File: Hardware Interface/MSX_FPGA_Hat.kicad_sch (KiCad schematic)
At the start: 24 parts, among them J1 J1, J2 J2, J3a1 J3a, J3b1 J3b, J4a1 J4a, J4b1 J4b, U1 74LVC245A, U2 74LVC245A, U3 74LVC245A, U4 74LVC245A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

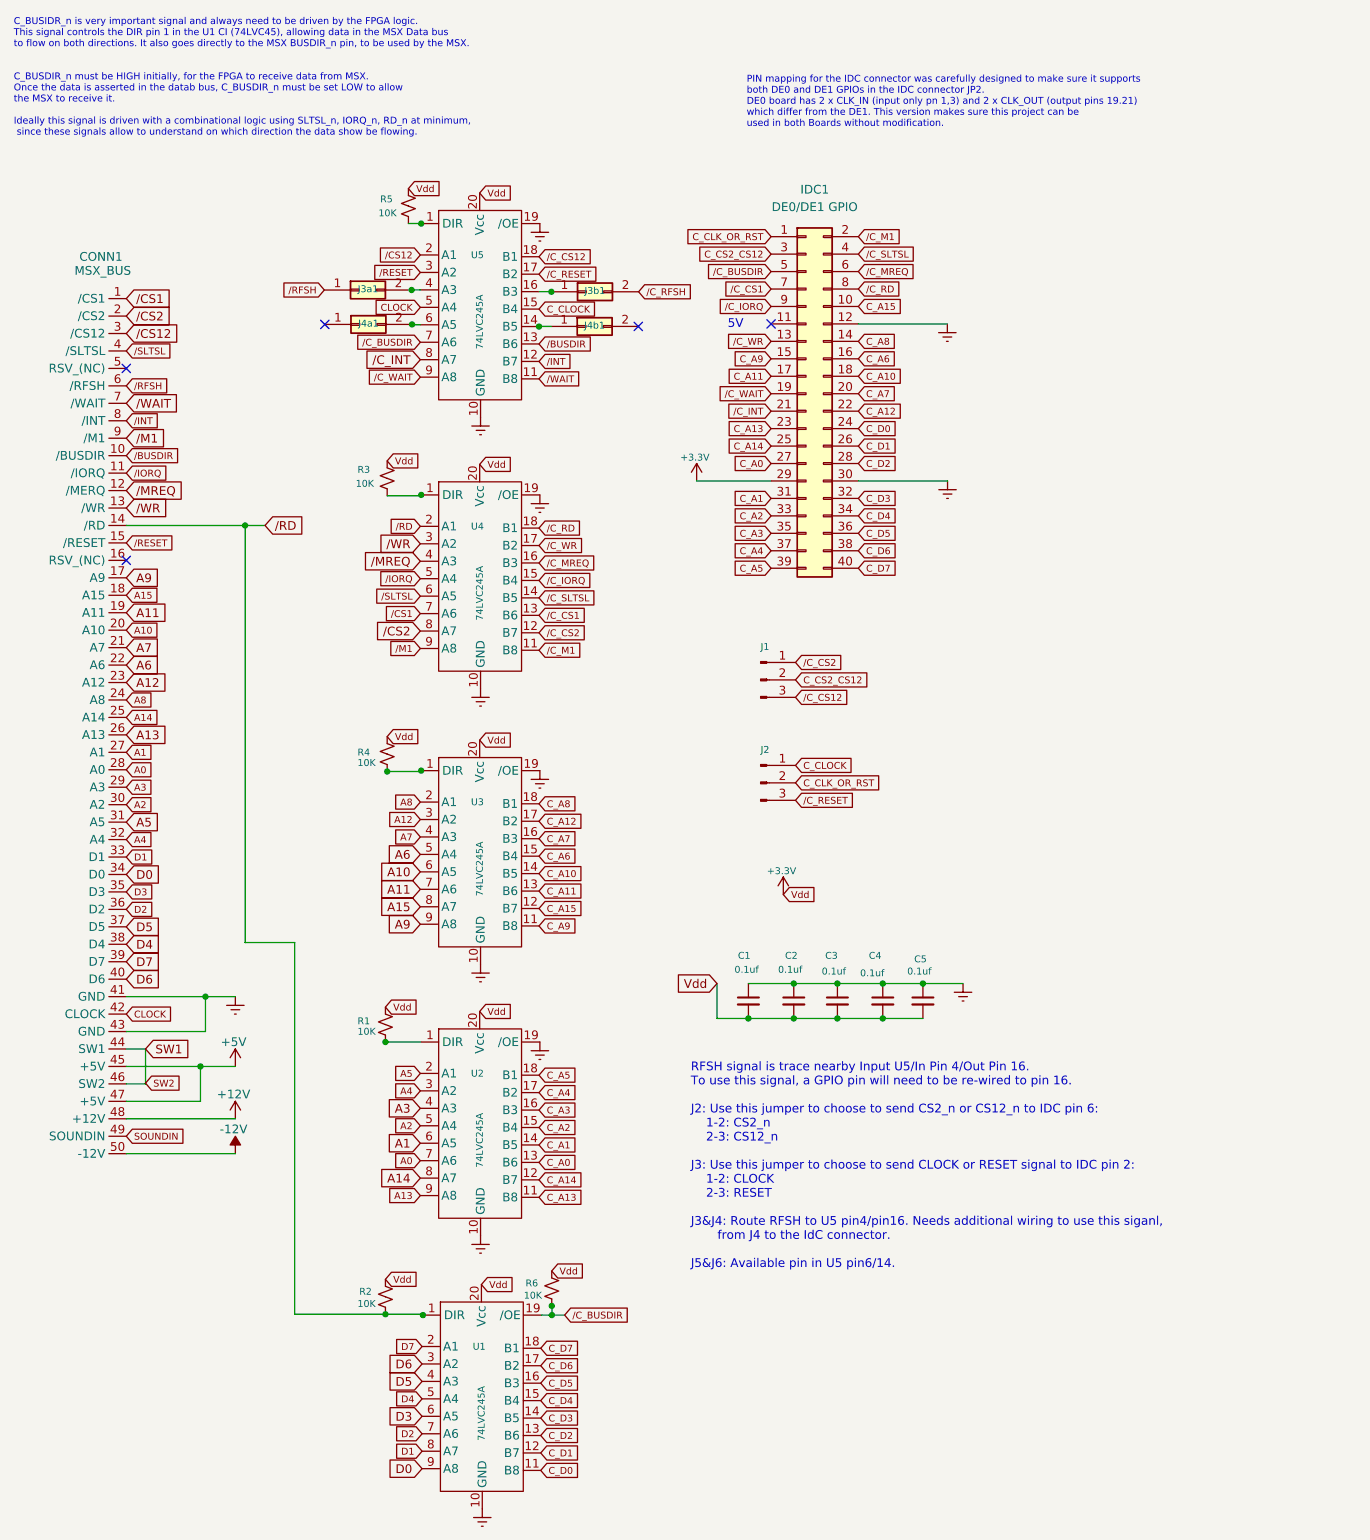
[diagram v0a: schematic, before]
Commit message: Moving to version 1.2 as it's clear that the OD pin in the U1 is not being driven correctly and need a separate pin for this purpose. V1.2 has this change implemented
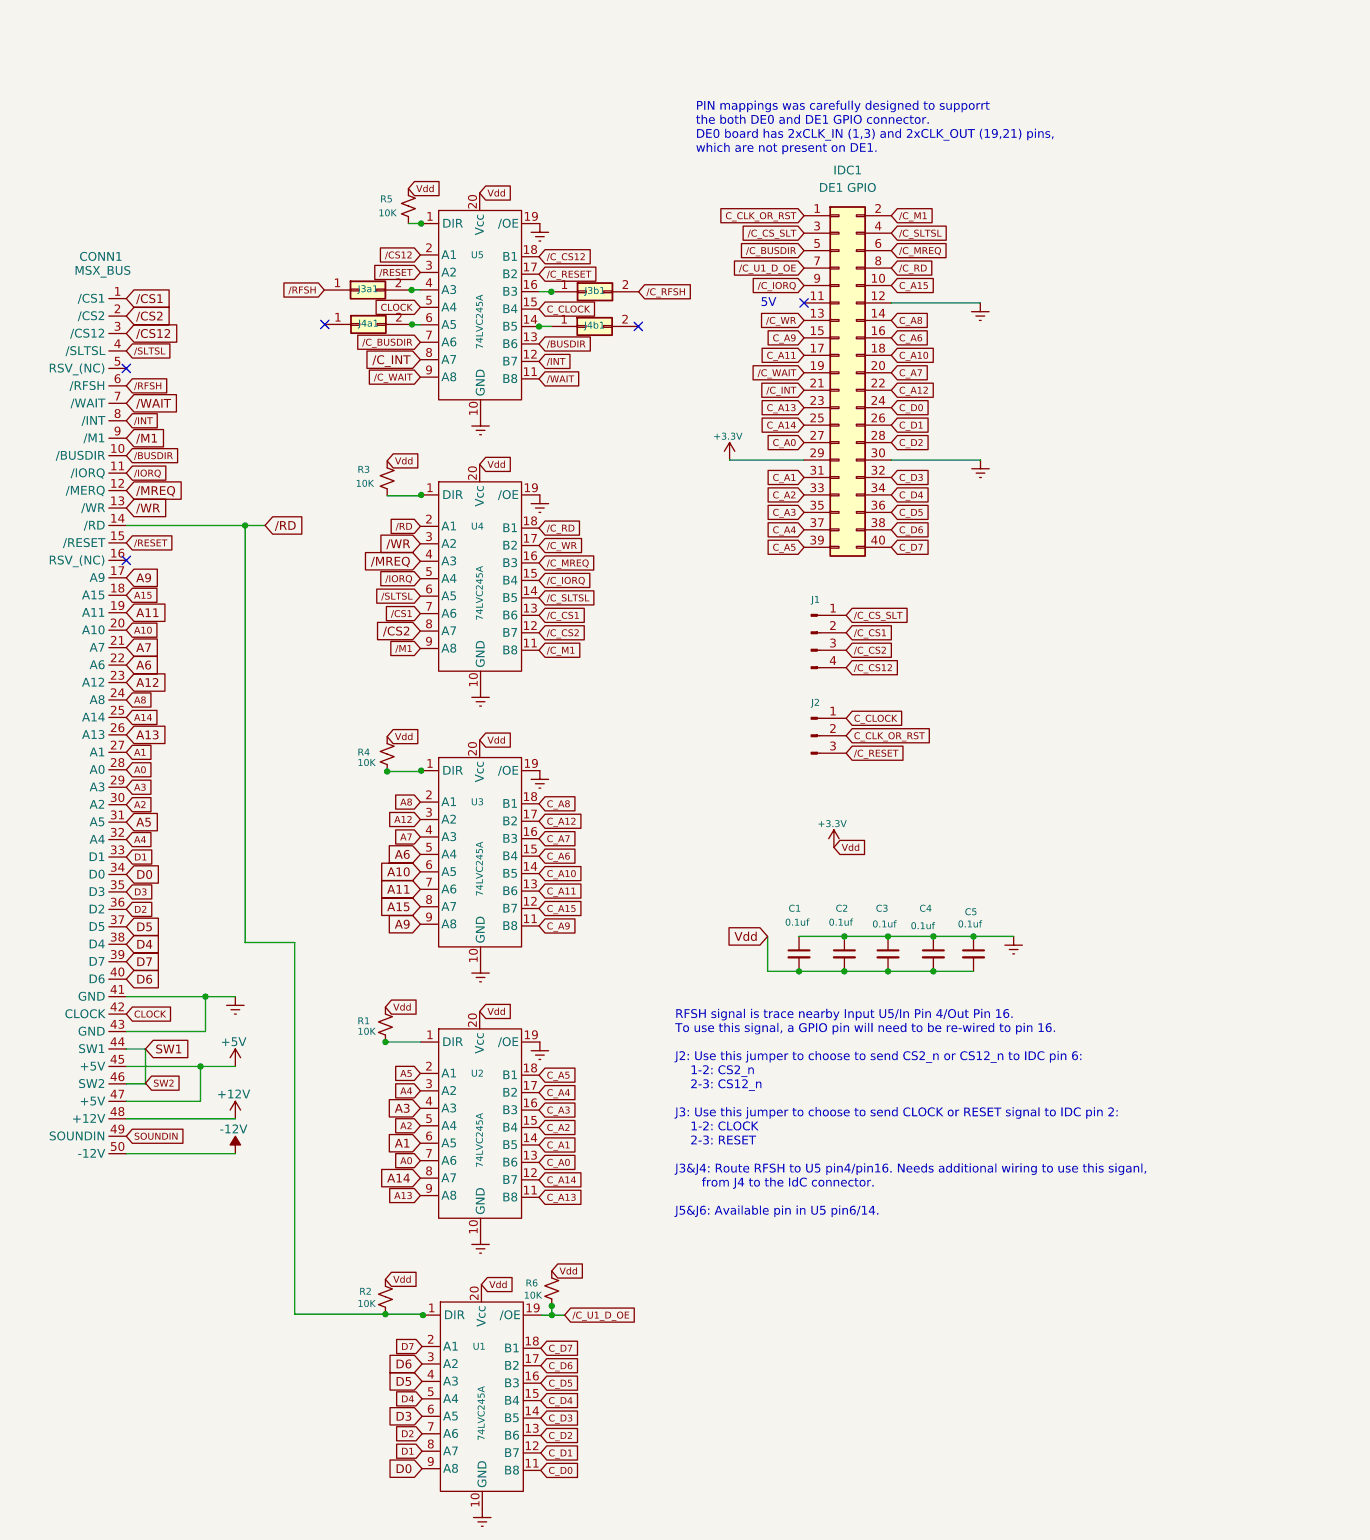
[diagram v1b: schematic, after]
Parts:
- IDC1: value DE0/DE1 GPIO -> DE1 GPIO
- J1: footprint Connector_PinHeader_2.54mm:PinHeader_1x03_P2.54mm_Vertical -> Connector_PinHeader_2.54mm:PinHeader_2x02_P2.54mm_Vertical; symbol Connector:Conn_01x03_Male -> Connector:Conn_01x04_Male
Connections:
- net /C_BUSDIR: no longer R6.2, U1.19 (/OE)
- net /C_CS1: now also J1.2 (Pin_2); no longer IDC1.7 (Pin_7)
- net /C_CS12: now also J1.4 (Pin_4); no longer J1.3 (Pin_3)
- net /C_CS2: now also J1.3 (Pin_3); no longer J1.1 (Pin_1)
- net C_CS2_CS12 renamed /C_CS_SLT
- net /C_CS_SLT: now also J1.1 (Pin_1); no longer J1.2 (Pin_2)
- new net /C_U1_D_OE: IDC1.7 (Pin_7), R6.2, U1.19 (/OE)
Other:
- note added: "PIN mappings was carefully designed to supporrt the both DE0 and DE1 GPIO connector. DE0 board has 2xCLK_IN (1,3) and 2xCLK_OUT (19,21) pins, which are not present on DE1."
- note removed: "C_BUSIDR_n is very important signal and always need to be driven by the FPGA logic. This signal controls the DIR pin 1 in the U1 CI (74LVC45), allowing data in the MSX Data bus to flow on both directions. It also goes directly to the MSX BUSDIR_n pin, to be used by the MSX. C_BUSDIR_n must be HIGH initially, for the FPGA to receive data from MSX. Once the data is asserted in the datab bus, C_BUSD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"
- note removed: "PIN mapping for the IDC connector was carefully designed to make sure it supports both DE0 and DE1 GPIOs in the IDC connector JP2. DE0 board has 2 x CLK_IN (input only pn 1,3) and 2 x CLK_OUT (output pins 19.21) which differ from the DE1. This version makes sure this project can be used in both Boards without modification."
- moved on the sheet: C1, C2, C3, C4, C5, IDC1, J2

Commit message: Added proper readme
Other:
- note added: "/C_U1_D_OE pin must be asserted according to the direction of data in the MSX Data Bus (U1 in the interface)"
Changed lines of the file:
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@@
+    (effects (font (size 1.27 1.27)) (justify left bottom))
+  )
+  (text "/C_U1_D_OE pin must be asserted according to the direction of data \nin the MSX Data Bus (U1 in the interface)"
+    (at 113.538 21.336 0)
     (effects (font (size 1.27 1.27)) (justify left bottom))
   )
